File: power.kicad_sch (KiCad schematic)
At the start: 18 parts, among them U2 AOZ1280CI, U3 LM1117-3.3, U4 LM321

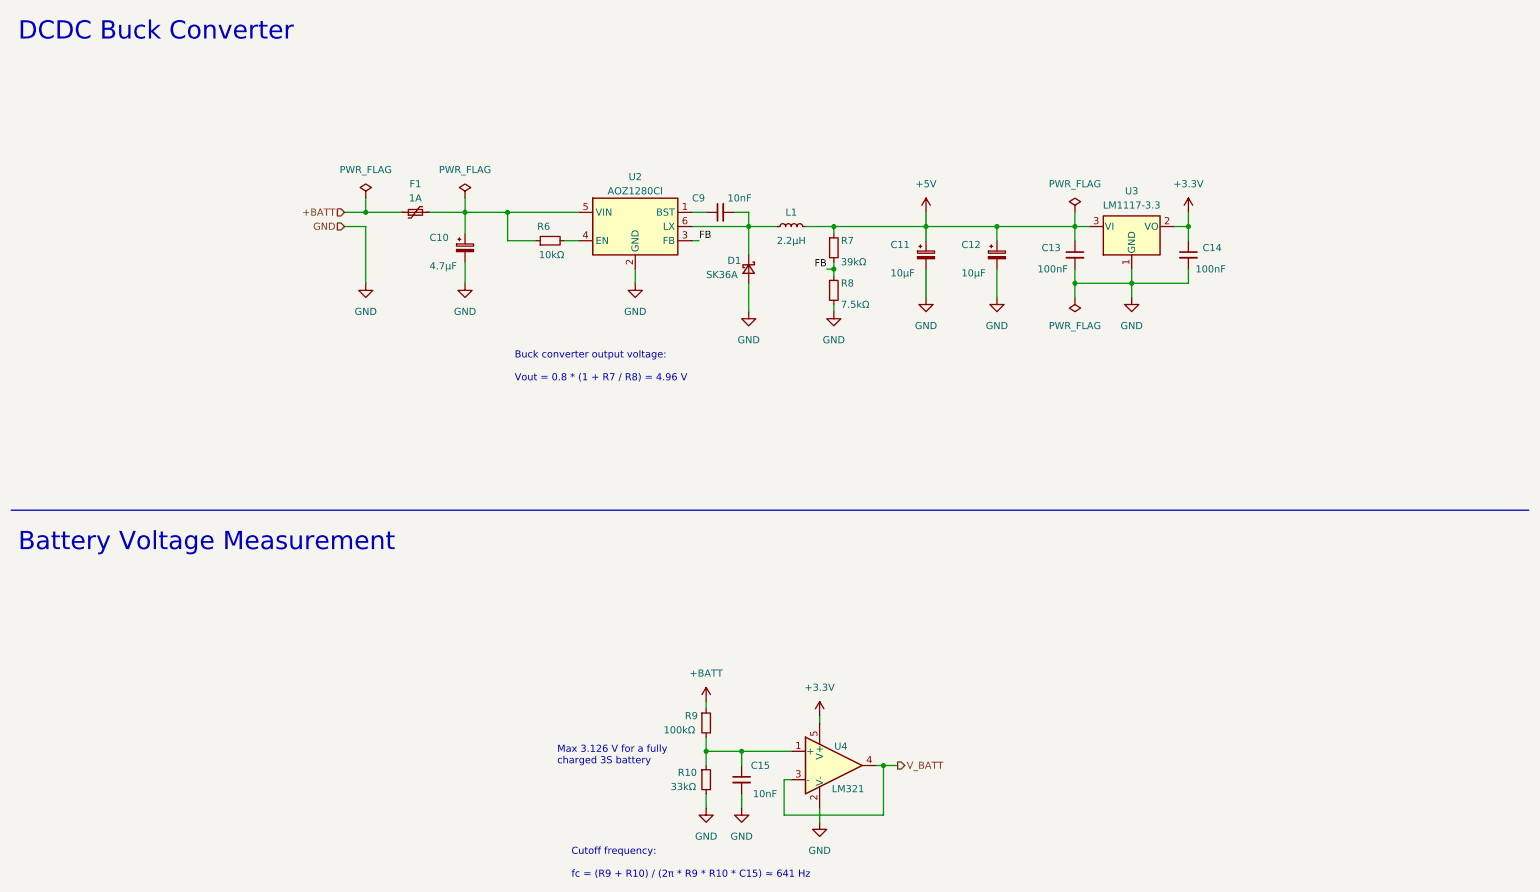
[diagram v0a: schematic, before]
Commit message: Route PCB tracks
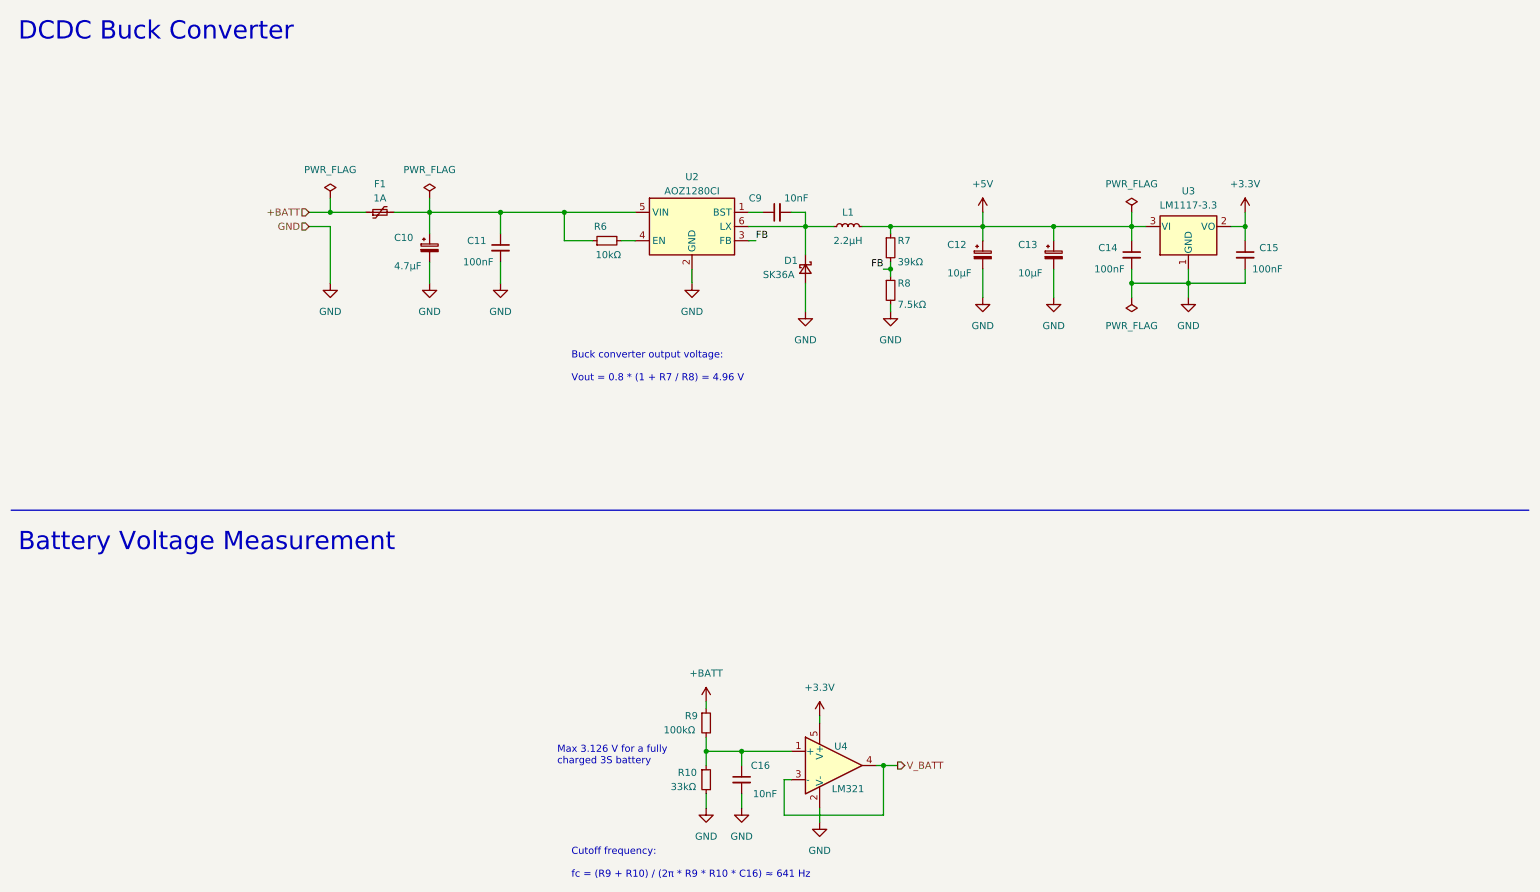
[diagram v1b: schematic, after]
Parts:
- added C11: 100nF, Capacitor_SMD:C_0603_1608Metric, symbol Device:C_Small
- renumbered C11 to C12, C12 to C13, C13 to C14, C14 to C15, C15 to C16
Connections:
- net GND: now also C11.2
- net at C10.1, F1.2, R6.1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: now also C11.1
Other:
- note added: "Cutoff frequency: fc = (R9 + R10) / (2π * R9 * R10 * C16) ≈ 641 Hz"
- note removed: "Cutoff frequency: fc = (R9 + R10) / (2π * R9 * R10 * C15) ≈ 641 Hz"
- moved on the sheet: C10, C12, C13, C14, C15, C9, D1, F1, L1, R6, R7, R8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
